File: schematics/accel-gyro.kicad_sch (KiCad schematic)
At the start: 2 parts, among them U5 Accel / Gyro

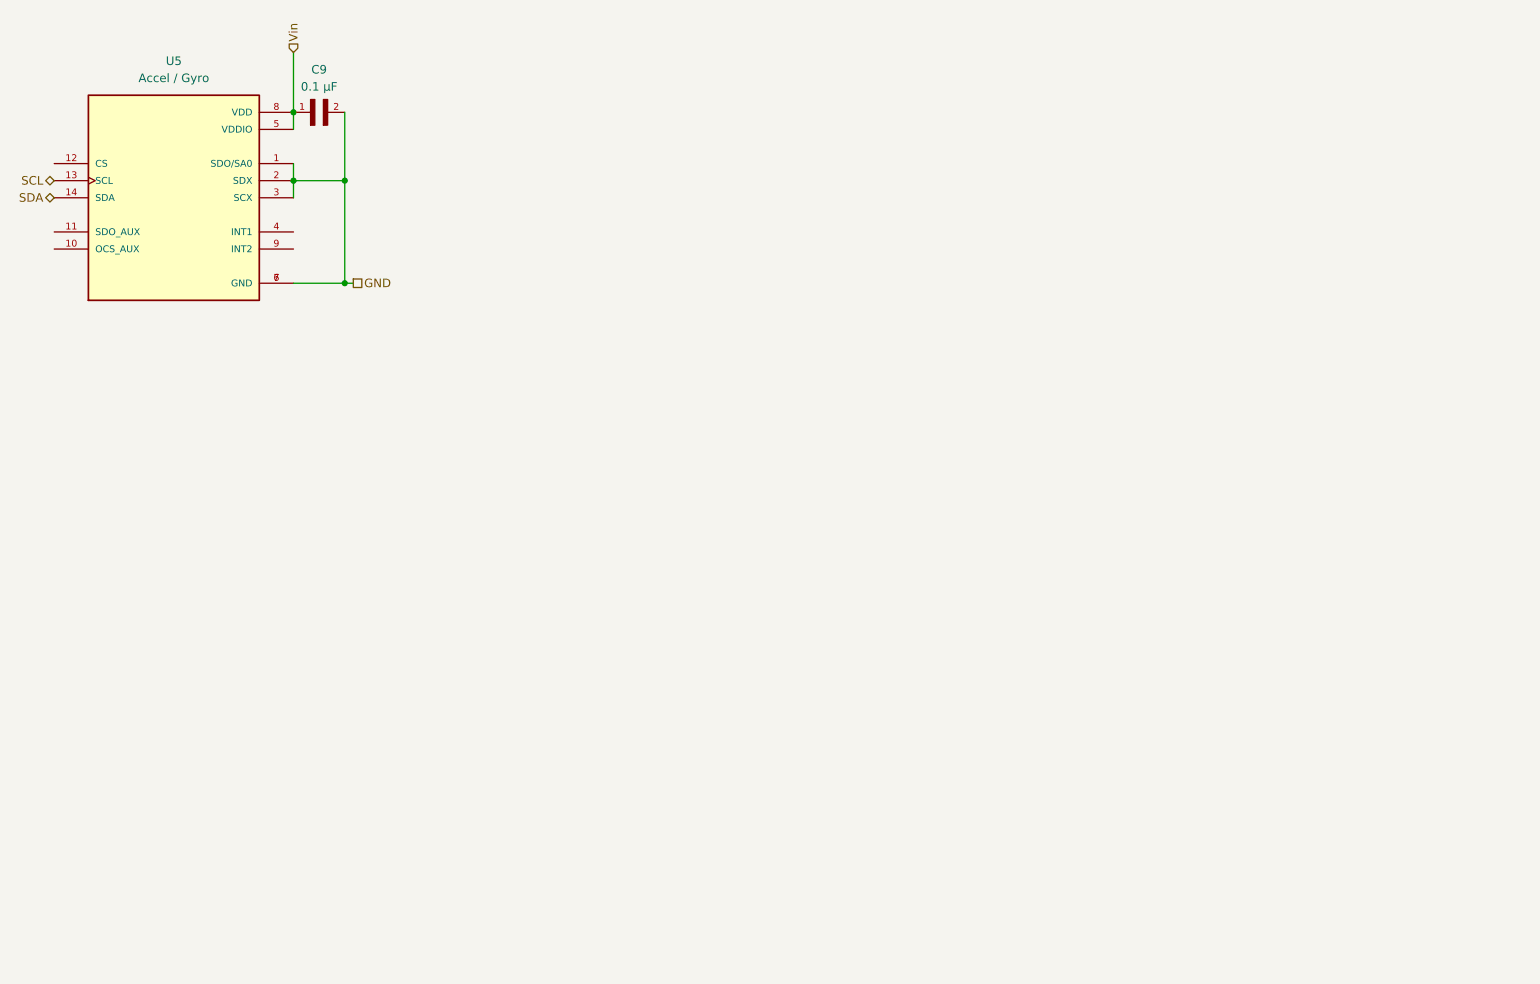
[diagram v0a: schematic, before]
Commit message: Added accel/gyro sheet title
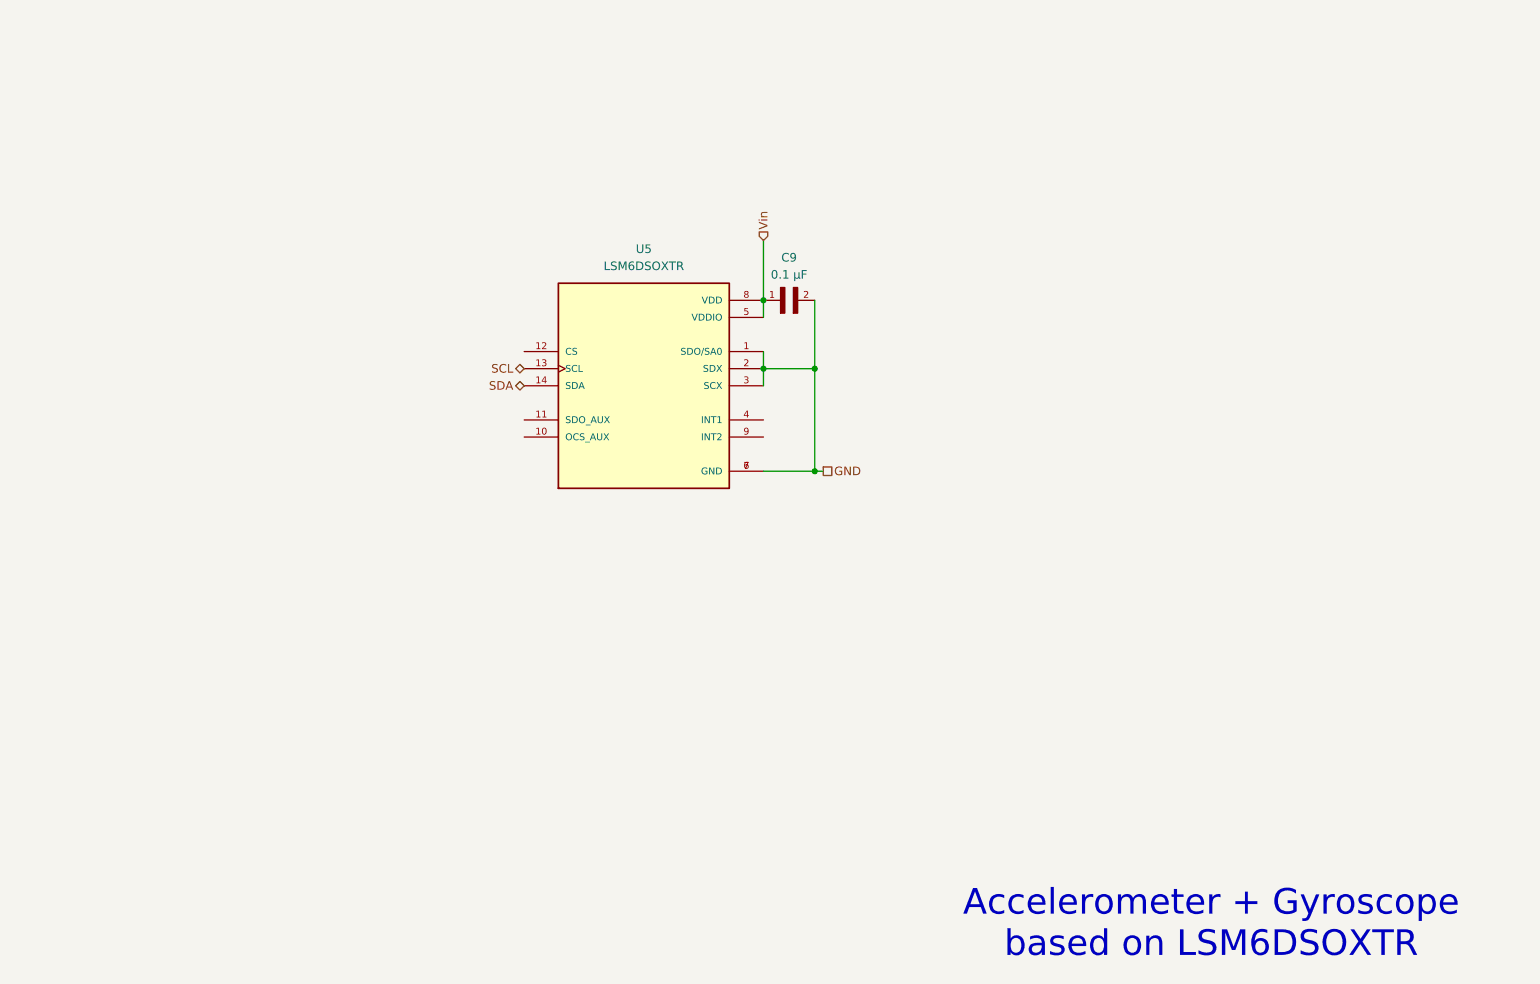
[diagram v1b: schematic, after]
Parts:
- U5: value Accel / Gyro -> LSM6DSOXTR
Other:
- note added: "Accelerometer + Gyroscope based on LSM6DSOXTR"
- moved on the sheet: C9, U5
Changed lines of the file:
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@@
 	(generator_version "9.0")
 	(paper "A4")
+	(text "Accelerometer + Gyroscope\nbased on LSM6DSOXTR"
+		(exclude_from_sim no)
+		(at 231.648 173.99 0)
+		(effects
+			(font
+				(size 3.81 3.81)
+			)
+		)
+	)
 	(junction
-		(at 95.25 63.5)
+		(at 165.1 91.44)
 		(diameter 0)
 		(color 0 0 0 0)
 	)
 	(junction
-		(at 102.87 78.74)
+		(at 172.72 106.68)
 		(diameter 0)
 		(color 0 0 0 0)
 	)
 	(junction
-		(at 95.25 53.34)
+		(at 165.1 81.28)
 		(diameter 0)
 		(color 0 0 0 0)
 	)
 	(junction
-		(at 102.87 63.5)
+		(at 172.72 91.44)
 		(diameter 0)
 		(color 0 0 0 0)
@@
 	(wire
 		(pts
-			(xy 102.87 53.34) (xy 102.87 63.5)
-		)
-		(stroke
-			(width 0)
-			(type default)
-		)
-	)
-	(wire
-		(pts
-			(xy 95.25 78.74) (xy 102.87 78.74)
-		)
-		(stroke
-			(width 0)
-			(type default)
-		)
-	)
-	(wire
-		(pts
-			(xy 95.25 44.45) (xy 95.25 53.34)
-		)
-		(stroke
-			(width 0)
-			(type default)
-		)
-	)
-	(wire
-		(pts
-			(xy 102.87 78.74) (xy 104.14 78.74)
-		)
-		(stroke
-			(width 0)
-			(type default)
-		)
-	)
-	(wire
-		(pts
-			(xy 95.25 63.5) (xy 95.25 66.04)
-		)
-		(stroke
-			(width 0)
-			(type default)
-		)
-	)
-	(wire
-		(pts
-			(xy 95.25 63.5) (xy 102.87 63.5)
-		)
-		(stroke
-			(width 0)
-			(type default)
-		)
-	)
-	(wire
-		(pts
-			(xy 95.25 60.96) (xy 95.25 63.5)
-		)
-		(stroke
-			(width 0)
-			(type default)
-		)
-	)
-	(wire
-		(pts
-			(xy 95.25 53.34) (xy 95.25 55.88)
-		)
-		(stroke
-			(width 0)
-			(type default)
-		)
-	)
-	(wire
-		(pts
-			(xy 102.87 63.5) (xy 102.87 78.74)
+			(xy 172.72 81.28) (xy 172.72 91.44)
+		)
+		(stroke
+			(width 0)
+			(type default)
+		)
+	)
+	(wire
+		(pts
+			(xy 165.1 106.68) (xy 172.72 106.68)
+		)
+		(stroke
+			(width 0)
+			(type default)
+		)
+	)
+	(wire
+		(pts
+			(xy 165.1 72.39) (xy 165.1 81.28)
+		)
+		(stroke
+			(width 0)
+			(type default)
+		)
+	)
+	(wire
+		(pts
+			(xy 172.72 106.68) (xy 173.99 106.68)
+		)
+		(stroke
+			(width 0)
+			(type default)
+		)
+	)
+	(wire
+		(pts
+			(xy 165.1 91.44) (xy 165.1 93.98)
+		)
+		(stroke
+			(width 0)
+			(type default)
+		)
+	)
+	(wire
+		(pts
+			(xy 165.1 91.44) (xy 172.72 91.44)
+		)
+		(stroke
+			(width 0)
+			(type default)
+		)
+	)
+	(wire
+		(pts
+			(xy 165.1 88.9) (xy 165.1 91.44)
+		)
+		(stroke
+			(width 0)
+			(type default)
+		)
+	)
+	(wire
+		(pts
+			(xy 165.1 81.28) (xy 165.1 83.82)
+		)
+		(stroke
+			(width 0)
+			(type default)
+		)
+	)
+	(wire
+		(pts
+			(xy 172.72 91.44) (xy 172.72 106.68)
 		)
 		(stroke
@@
 	(hierarchical_label "GND"
 		(shape passive)
-		(at 104.14 78.74 0)
+		(at 173.99 106.68 0)
 		(effects
 			(font
@@
 	(hierarchical_label "Vin"
 		(shape input)
-		(at 95.25 44.45 90)
+		(at 165.1 72.39 90)
 		(effects
 			(font
@@
 	(hierarchical_label "SCL"
 		(shape bidirectional)
-		(at 59.69 63.5 180)
+		(at 129.54 91.44 180)
 		(effects
 			(font
@@
 	(hierarchical_label "SDA"
 		(shape bidirectional)
-		(at 59.69 66.04 180)
+		(at 129.54 93.98 180)
 		(effects
 			(font
@@
 	(symbol
 		(lib_id "LSM6DSOXTR:LSM6DSOXTR")
-		(at 77.47 66.04 0)
+		(at 147.32 93.98 0)
 		(unit 1)
 		(exclude_from_sim no)
@@
 		(fields_autoplaced yes)
 		(property "Reference" "U5"
-			(at 77.47 45.72 0)
-			(effects
-				(font
-					(size 1.27 1.27)
-				)
-			)
-		)
-		(property "Value" "Accel / Gyro"
-			(at 77.47 48.26 0)
+			(at 147.32 73.66 0)
+			(effects
+				(font
+					(size 1.27 1.27)
+				)
+			)
+		)
+		(property "Value" "LSM6DSOXTR"
+			(at 147.32 76.2 0)
 			(effects
 				(font
@@
 		)
 		(property "Footprint" "LSM6DSOXTR:PQFN50P250X300X86-14N"
-			(at 77.47 66.04 0)
+			(at 147.32 93.98 0)
 			(effects
 				(font
@@
 		)
 		(property "Datasheet" ""
-			(at 77.47 66.04 0)
+			(at 147.32 93.98 0)
 			(effects
 				(font
@@
 		)
 		(property "Description" ""
-			(at 77.47 66.04 0)
+			(at 147.32 93.98 0)
 			(effects
 				(font
@@
 		)
 		(property "MF" "STMicroelectronics"
-			(at 77.47 66.04 0)
+			(at 147.32 93.98 0)
 			(effects
 				(font
@@
 		)
 		(property "Description_1" "Accelerometer, Gyroscope, 6 Axis Sensor I2C, SPI Output"
-			(at 77.47 66.04 0)
+			(at 147.32 93.98 0)
 			(effects
 				(font
@@
 		)
 		(property "Package" "VFLGA-14 STMicroelectronics"
-			(at 77.47 66.04 0)
+			(at 147.32 93.98 0)
 			(effects
 				(font
@@
 		)
 		(property "Price" "None"
-			(at 77.47 66.04 0)
+			(at 147.32 93.98 0)
 			(effects
 				(font
@@
 		)
 		(property "Check_prices" "https://www.snapeda.com/parts/LSM6DSOXTR/STMicroelectronics/view-part/?ref=eda"
-			(at 77.47 66.04 0)
+			(at 147.32 93.98 0)
 			(effects
 				(font
@@
 		)
 		(property "STANDARD" "IPC7351B"
-			(at 77.47 66.04 0)
+			(at 147.32 93.98 0)
 			(effects
 				(font
@@
 		)
 		(property "PARTREV" "3.0"
-			(at 77.47 66.04 0)
+			(at 147.32 93.98 0)
 			(effects
 				(font
@@
 		)
 		(property "SnapEDA_Link" "https://www.snapeda.com/parts/LSM6DSOXTR/STMicroelectronics/view-part/?ref=snap"
-			(at 77.47 66.04 0)
+			(at 147.32 93.98 0)
 			(effects
 				(font
@@
 		)
 		(property "MP" "LSM6DSOXTR"
-			(at 77.47 66.04 0)
+			(at 147.32 93.98 0)
 			(effects
 				(font
@@
 		)
 		(property "Availability" "In Stock"
-			(at 77.47 66.04 0)
+			(at 147.32 93.98 0)
 			(effects
 				(font
@@
 		)
 		(property "MANUFACTURER" "ST Microelectronics"
-			(at 77.47 66.04 0)
+			(at 147.32 93.98 0)
 			(effects
 				(font
@@
 	(symbol
 		(lib_id "MBJCG168BB7104KTPA18:MBJCG168BB7104KTPA18")
-		(at 97.79 53.34 0)
+		(at 167.64 81.28 0)
 		(unit 1)
 		(exclude_from_sim no)
@@
 		(fields_autoplaced yes)
 		(property "Reference" "C9"
-			(at 99.06 46.99 0)
+			(at 168.91 74.93 0)
 			(effects
 				(font
@@
 		)
 		(property "Value" "0.1 µF"
-			(at 99.06 49.53 0)
+			(at 168.91 77.47 0)
 			(effects
 				(font
@@
 		)
 		(property "Footprint" "MBJCG168BB7104KTPA18:CAPC1608X100N"
-			(at 97.79 53.34 0)
+			(at 167.64 81.28 0)
 			(effects
 				(font
@@
 		)
 		(property "Datasheet" ""
-			(at 97.79 53.34 0)
+			(at 167.64 81.28 0)
 			(effects
 				(font
@@
 		)
 		(property "Description" ""
-			(at 97.79 53.34 0)
+			(at 167.64 81.28 0)
 			(effects
 				(font
@@
 		)
 		(property "MF" "Taiyo Yuden"
-			(at 97.79 53.34 0)
+			(at 167.64 81.28 0)
 			(effects
 				(font
@@
 		)
 		(property "MAXIMUM_PACKAGE_HEIGHT" "1.00mm"
-			(at 97.79 53.34 0)
+			(at 167.64 81.28 0)
 			(effects
 				(font
@@
 		)
 		(property "Package" "1608-2 TAIYO"
-			(at 97.79 53.34 0)
+			(at 167.64 81.28 0)
 			(effects
 				(font
@@
 		)
 		(property "Price" "None"
-			(at 97.79 53.34 0)
+			(at 167.64 81.28 0)
 			(effects
 				(font
@@
 		)
 		(property "Check_prices" "https://www.snapeda.com/parts/MBJCG168BB7104KTPA18/Taiyo+Yuden/view-part/?ref=eda"
-			(at 97.79 53.34 0)
+			(at 167.64 81.28 0)
 			(effects
 				(font
@@
 		)
 		(property "STANDARD" "IPC-7351B"
-			(at 97.79 53.34 0)
+			(at 167.64 81.28 0)
 			(effects
 				(font
@@
 		)
 		(property "PARTREV" "NA"
-			(at 97.79 53.34 0)
+			(at 167.64 81.28 0)
 			(effects
 				(font
@@
 		)
 		(property "SnapEDA_Link" "https://www.snapeda.com/parts/MBJCG168BB7104KTPA18/Taiyo+Yuden/view-part/?ref=snap"
-			(at 97.79 53.34 0)
+			(at 167.64 81.28 0)
 			(effects
 				(font
@@
 		)
 		(property "MP" "MBJCG168BB7104KTPA18"
-			(at 97.79 53.34 0)
+			(at 167.64 81.28 0)
 			(effects
 				(font
@@
 		)
 		(property "Description_1" "0.1uF 35V 10% Multilayer Ceramic Capacitor X7R 0603 (1608 Metric)"
-			(at 97.79 53.34 0)
+			(at 167.64 81.28 0)
 			(effects
 				(font
@@
 		)
 		(property "Availability" "In Stock"
-			(at 97.79 53.34 0)
+			(at 167.64 81.28 0)
 			(effects
 				(font
@@
 		)
 		(property "MANUFACTURER" "Taiyo Yuden"
-			(at 97.79 53.34 0)
-			(effects
-				(font
+			(at 167.64 81.28 0)
+			(effects
+				(font

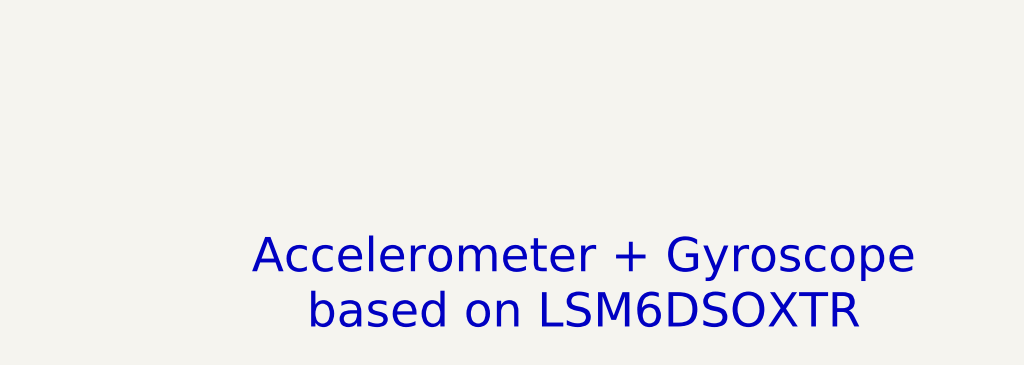
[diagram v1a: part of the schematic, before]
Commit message: Normalized sheet titles; added MMCX connector for GPS antenna + active antenna power switch
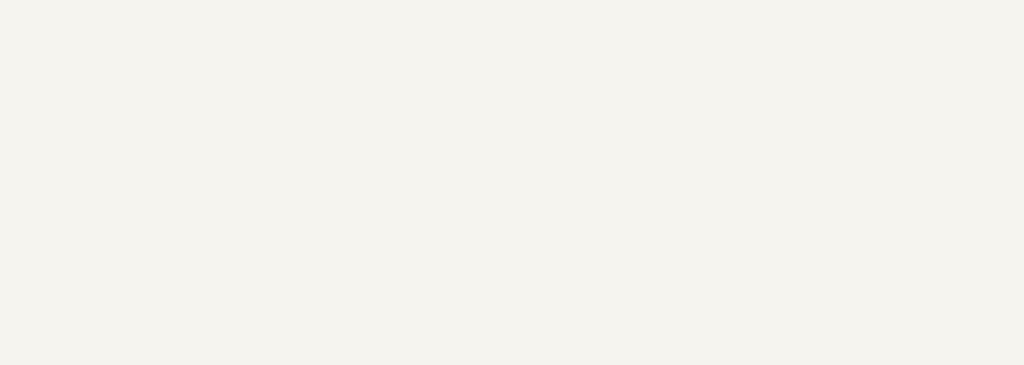
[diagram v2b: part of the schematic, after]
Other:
- note removed: "Accelerometer + Gyroscope based on LSM6DSOXTR"
- title: (none) -> Accelerometer + Gyroscope based on LSM6DSOXTR
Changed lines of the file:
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@@
 	(generator_version "9.0")
 	(paper "A4")
-	(text "Accelerometer + Gyroscope\nbased on LSM6DSOXTR"
-		(exclude_from_sim no)
-		(at 231.648 173.99 0)
-		(effects
-			(font
-				(size 3.81 3.81)
-			)
-		)
+	(title_block
+		(title "Accelerometer + Gyroscope based on LSM6DSOXTR")
+		(comment 1 "Currently in MODE 1")
+		(comment 2 "MODE 2 allows the integration of a magnometer")
 	)
 	(junction

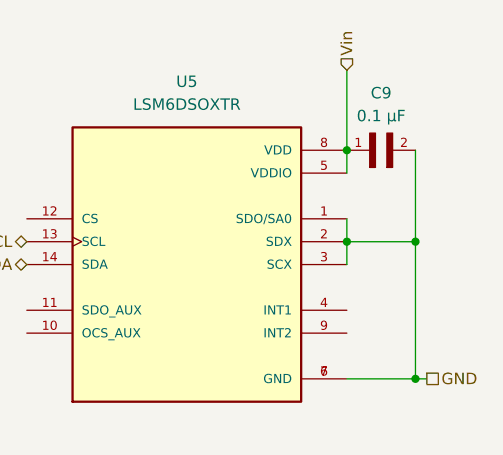
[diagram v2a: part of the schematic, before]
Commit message: Include GND in each schema sub-pages
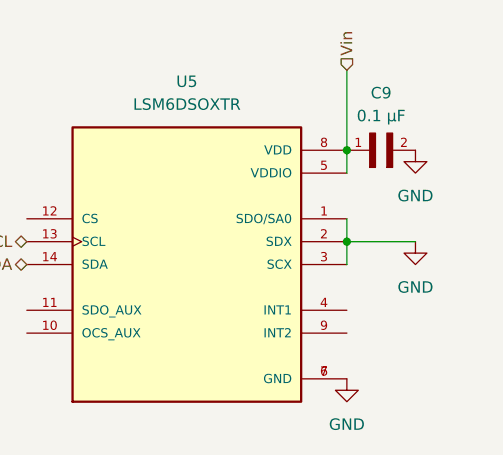
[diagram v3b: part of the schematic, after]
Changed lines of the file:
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@@
-	)
-	(junction
-		(at 172.72 106.68)
-		(diameter 0)
-		(color 0 0 0 0)
 	)
 	(junction
@@
 		(color 0 0 0 0)
 	)
-	(junction
-		(at 172.72 91.44)
-		(diameter 0)
-		(color 0 0 0 0)
-	)
-	(wire
-		(pts
-			(xy 172.72 81.28) (xy 172.72 91.44)
-		)
-		(stroke
-			(width 0)
-			(type default)
-		)
-	)
-	(wire
-		(pts
-			(xy 165.1 106.68) (xy 172.72 106.68)
-		)
-		(stroke
-			(width 0)
-			(type default)
-		)
-	)
 	(wire
 		(pts
@@
 	(wire
 		(pts
-			(xy 172.72 106.68) (xy 173.99 106.68)
-		)
-		(stroke
-			(width 0)
-			(type default)
-		)
-	)
-	(wire
-		(pts
 			(xy 165.1 91.44) (xy 165.1 93.98)
 		)
@@
 			(width 0)
 			(type default)
-		)
-	)
-	(wire
-		(pts
-			(xy 172.72 91.44) (xy 172.72 106.68)
-		)
-		(stroke
-			(width 0)
-			(type default)
-		)
-	)
-	(hierarchical_label "GND"
-		(shape passive)
-		(at 173.99 106.68 0)
-		(effects
-			(font
-				(size 1.27 1.27)
-			)
-			(justify left)
 		)
 	)
@@
 		)
 	)
+	(symbol
+		(lib_id "power:GND")
+		(at 172.72 91.44 0)
+		(unit 1)
+		(exclude_from_sim no)
+		(in_bom yes)
+		(on_board yes)
+		(dnp no)
+		(fields_autoplaced yes)
+		(property "Reference" "#PWR015"
+			(at 172.72 97.79 0)
+			(effects
+				(font
+					(size 1.27 1.27)
+				)
+				(hide yes)
+			)
+		)
+		(property "Value" "GND"
+			(at 172.72 96.52 0)
+			(effects
+				(font
+					(size 1.27 1.27)
+				)
+			)
+		)
+		(property "Footprint" ""
+			(at 172.72 91.44 0)
+			(effects
+				(font
+					(size 1.27 1.27)
+				)
+				(hide yes)
+			)
+		)
+		(property "Datasheet" ""
+			(at 172.72 91.44 0)
+			(effects
+				(font
+					(size 1.27 1.27)
+				)
+				(hide yes)
+			)
+		)
+		(property "Description" "Power symbol creates a global label with name \"GND\" , ground"
+			(at 172.72 91.44 0)
+			(effects
+				(font
+					(size 1.27 1.27)
+				)
+				(hide yes)
+			)
+		)
+		(pin "1"
+		)
+		(instances
+			(project "bike-sensors-logger"
+				(path "/2c1d9222-af16-428b-85a5-a3d420373d70/cfd34f19-b9c8-43fa-a529-56c363000dae"
+					(reference "#PWR015")
+					(unit 1)
+				)
+			)
+		)
+	)
+	(symbol
+		(lib_id "power:GND")
+		(at 172.72 81.28 0)
+		(unit 1)
+		(exclude_from_sim no)
+		(in_bom yes)
+		(on_board yes)
+		(dnp no)
+		(fields_autoplaced yes)
+		(property "Reference" "#PWR014"
+			(at 172.72 87.63 0)
+			(effects
+				(font
+					(size 1.27 1.27)
+				)
+				(hide yes)
+			)
+		)
+		(property "Value" "GND"
+			(at 172.72 86.36 0)
+			(effects
+				(font
+					(size 1.27 1.27)
+				)
+			)
+		)
+		(property "Footprint" ""
+			(at 172.72 81.28 0)
+			(effects
+				(font
+					(size 1.27 1.27)
+				)
+				(hide yes)
+			)
+		)
+		(property "Datasheet" ""
+			(at 172.72 81.28 0)
+			(effects
+				(font
+					(size 1.27 1.27)
+				)
+				(hide yes)
+			)
+		)
+		(property "Description" "Power symbol creates a global label with name \"GND\" , ground"
+			(at 172.72 81.28 0)
+			(effects
+				(font
+					(size 1.27 1.27)
+				)
+				(hide yes)
+			)
+		)
+		(pin "1"
+		)
+		(instances
+			(project "bike-sensors-logger"
+				(path "/2c1d9222-af16-428b-85a5-a3d420373d70/cfd34f19-b9c8-43fa-a529-56c363000dae"
+					(reference "#PWR014")
+					(unit 1)
+				)
+			)
+		)
+	)
+	(symbol
+		(lib_id "power:GND")
+		(at 165.1 106.68 0)
+		(unit 1)
+		(exclude_from_sim no)
+		(in_bom yes)
+		(on_board yes)
+		(dnp no)
+		(fields_autoplaced yes)
+		(property "Reference" "#PWR01"
+			(at 165.1 113.03 0)
+			(effects
+				(font
+					(size 1.27 1.27)
+				)
+				(hide yes)
+			)
+		)
+		(property "Value" "GND"
+			(at 165.1 111.76 0)
+			(effects
+				(font
+					(size 1.27 1.27)
+				)
+			)
+		)
+		(property "Footprint" ""
+			(at 165.1 106.68 0)
+			(effects
+				(font
+					(size 1.27 1.27)
+				)
+				(hide yes)
+			)
+		)
+		(property "Datasheet" ""
+			(at 165.1 106.68 0)
+			(effects
+				(font
+					(size 1.27 1.27)
+				)
+				(hide yes)
+			)
+		)
+		(property "Description" "Power symbol creates a global label with name \"GND\" , ground"
+			(at 165.1 106.68 0)
+			(effects
+				(font
+					(size 1.27 1.27)
+				)
+				(hide yes)
+			)
+		)
+		(pin "1"
+		)
+		(instances
+			(project "bike-sensors-logger"
+				(path "/2c1d9222-af16-428b-85a5-a3d420373d70/cfd34f19-b9c8-43fa-a529-56c363000dae"
+					(reference "#PWR01")
+					(unit 1)
+				)
+			)
+		)
+	)

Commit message: Refactor WIP
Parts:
- renumbered U5 to U2
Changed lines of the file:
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@@
 		(dnp no)
 		(fields_autoplaced yes)
-		(property "Reference" "U5"
+		(property "Reference" "U2"
 			(at 147.32 73.66 0)
 			(effects
@@
 			(project "bike-sensors-logger"
 				(path "/2c1d9222-af16-428b-85a5-a3d420373d70/cfd34f19-b9c8-43fa-a529-56c363000dae"
-					(reference "U5")
+					(reference "U2")
 					(unit 1)
 				)
